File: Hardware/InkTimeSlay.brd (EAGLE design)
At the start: 46 x 35 mm, 105 parts, among them IC1 BQ25180YBGR, IC2 DRV2605YZFR, IC3 BMA423, IC9 RT6160AWSC, J1 503480-2400, J2 TC2030-IDC, J4 KH-TYPE-C-16P, Q1 20V/4.2A/52mΩ/1.4W, Q3 SI1308EDL-T1-GE3, U1 NRF52840_QF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

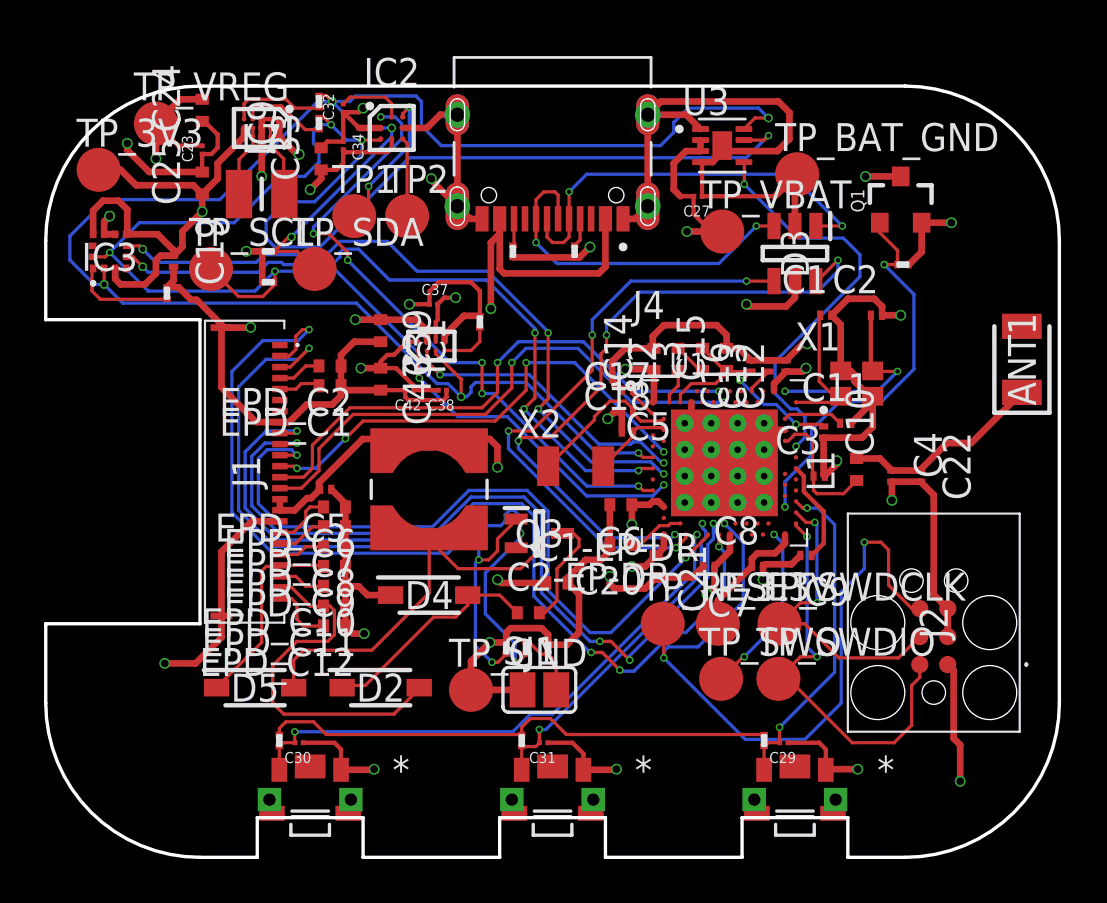
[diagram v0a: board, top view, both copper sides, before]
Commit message: 2D PCB changes
Got rid of 90 degree angles in wire routing, isolated the antenna better and surrounded its premises with GND vias, cropped the board under the antenna
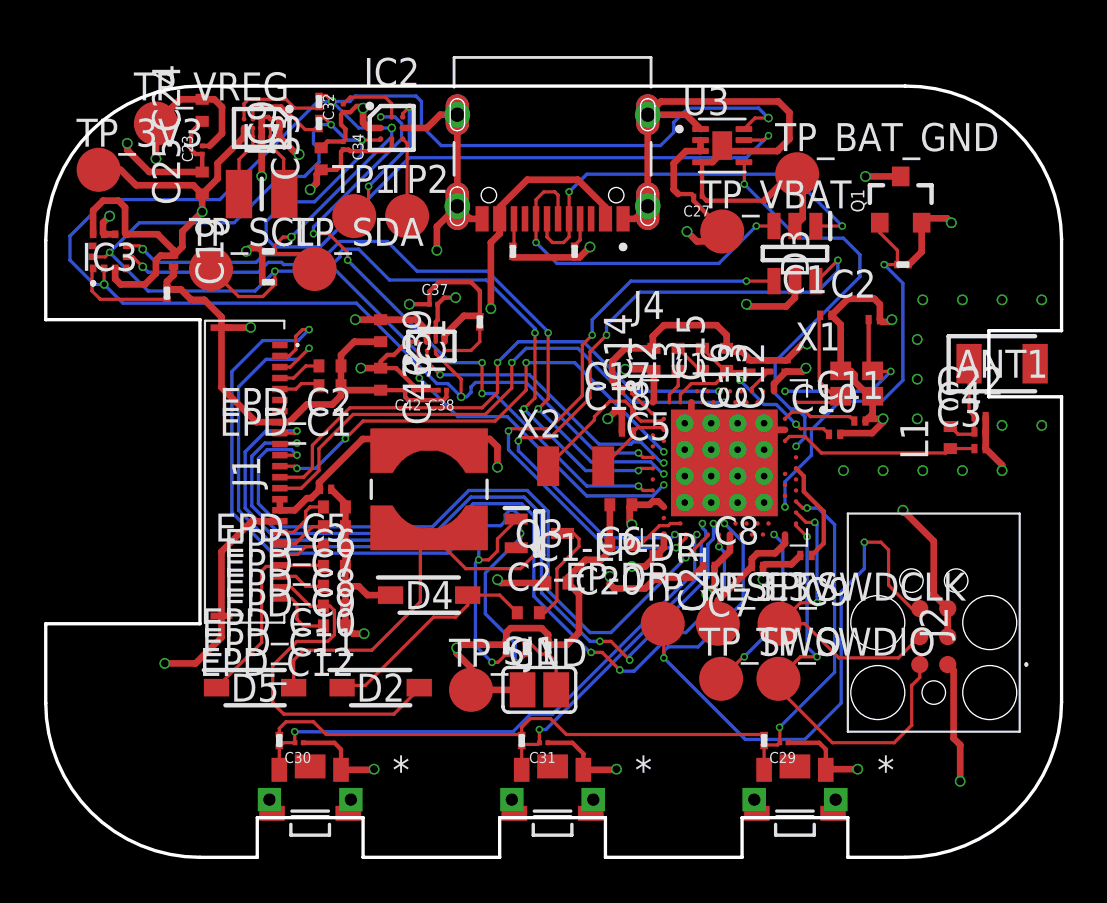
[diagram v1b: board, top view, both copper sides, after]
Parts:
- moved C3 7.41 mm to (19.4, 1.05)
- moved L1 4.49 mm to (18.1, 1.55)
- moved C4 4.47 mm to (19.4, 1.80), turned to 0 degrees
- moved C22 3.82 mm to (19.4, 2.50), turned to 0 degrees
- moved ANT1 0.92 mm to (20.4, 4.90), turned to 0 degrees
- moved C11 0.66 mm to (13.9, 2.30)
- moved C10 0.51 mm to (12.8, 1.70), turned to 0 degrees
- moved C2 0.22 mm to (14.6, 6.90)
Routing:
- net RF: track 9.22 -> 4.48 mm
- net N$20: track 6.03 -> 9.07 mm
- net VBUS: track 69.5 -> 67.0 mm
- net GND: track 193.6 -> 191.9 mm, vias 21 -> 35
- net VREG: track 33.5 -> 34.4 mm
- net N$28: track 9.17 -> 8.41 mm
- net N$24: track 2.74 -> 3.43 mm
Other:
- board size 46 x 35 mm -> 46.1 x 35 mm
